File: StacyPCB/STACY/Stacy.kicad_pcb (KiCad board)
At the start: 2 copper layers, 105.4 x 82.6 mm, 48 parts, among them J1 SOL, J10 kill, J11 ext3, J12 push_start, J13 relays, J14 door_lock, J15 ble_hm-10, J16 door_nano, J4 ext4, J5 ext0, J6 ext1, J7 USB_B_Micro, J8 SWD Debug, J9 ext2, SW1 SW_Push, U1 ATSAMD21G18A-AUT, U2 TPS62163DSG, Y1 16MHz

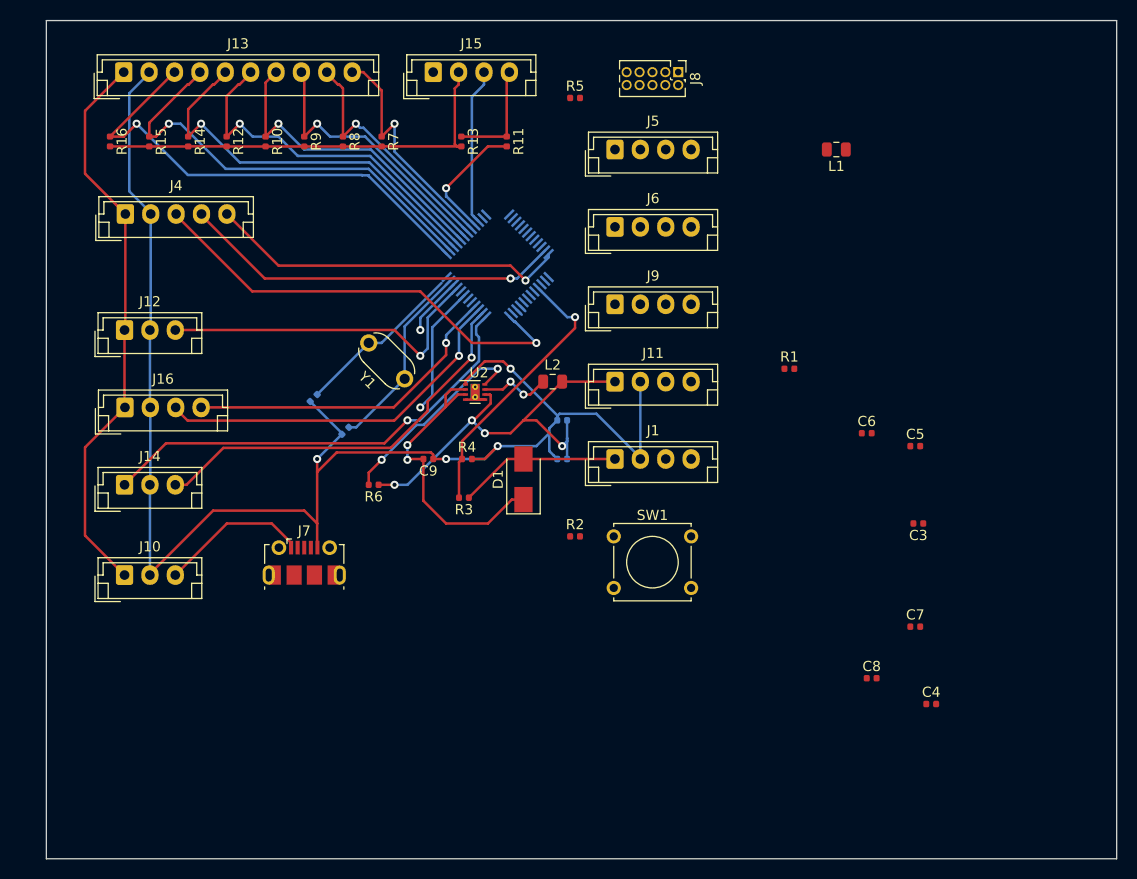
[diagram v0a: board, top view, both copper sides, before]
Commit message: Routed all decoupling caps and fixed clock footprint. This version has been manufactured
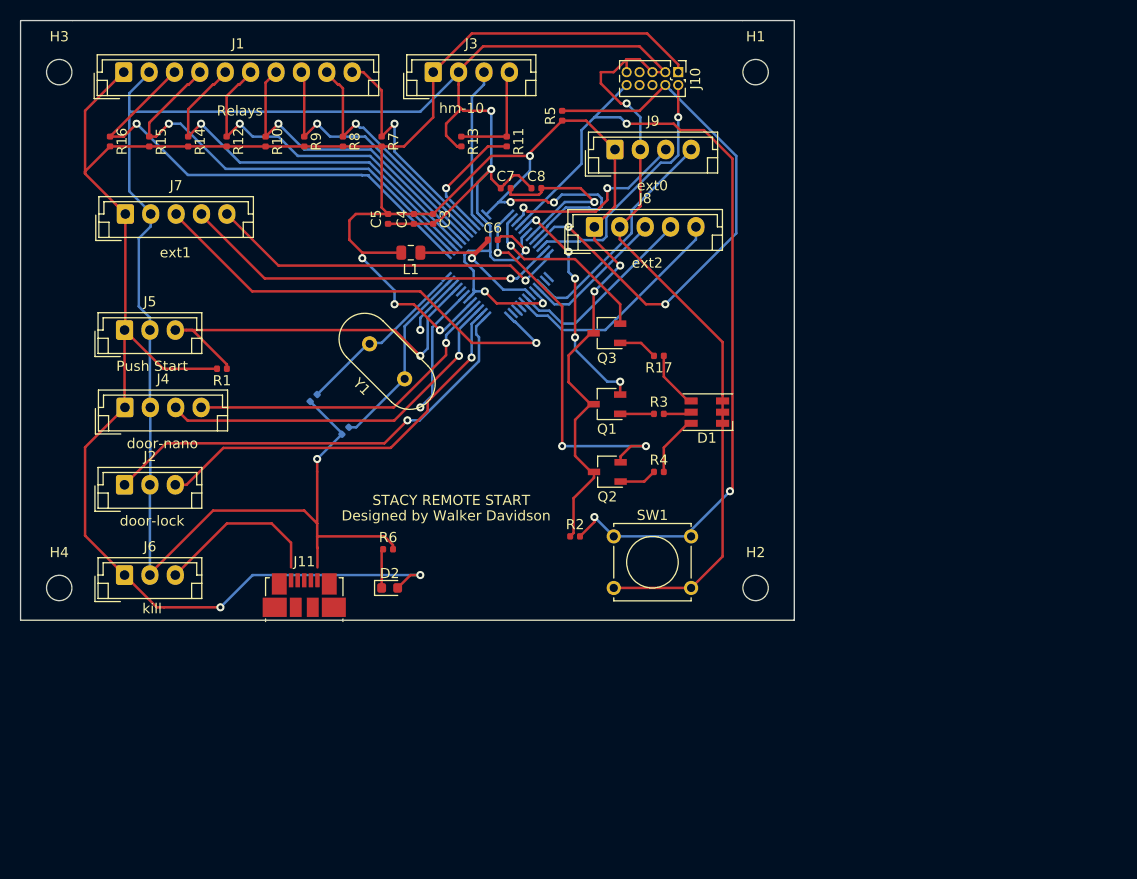
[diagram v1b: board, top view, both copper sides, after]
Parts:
- removed C10, C11, C9: 10u, Capacitor_SMD:C_0402_1005Metric
- removed the J1 at (166.5, 88.9)
- removed the J6 at (166.5, 66.0)
- removed the J7 at (135.9, 99.1)
- removed the J9 at (166.5, 73.7)
- removed L2: 2.2u, Inductor_SMD:L_0805_2012Metric
- removed U2: TPS62163DSG, Package_SON:WSON-8-1EP_2x2mm_P0.5mm_EP0.9x1.6mm_ThermalVias
- added D2: LED, LED_SMD:LED_0603_1608Metric, F.Cu at (144.3, 101.6)
- added H1: MountingHole, MountingHole:MountingHole_2.5mm, F.Cu at (180.3, 50.8)
- added H2: MountingHole, MountingHole:MountingHole_2.5mm, F.Cu at (180.3, 101.6)
- added H3: MountingHole, MountingHole:MountingHole_2.5mm, F.Cu at (111.8, 50.8)
- added H4: MountingHole, MountingHole:MountingHole_2.5mm, F.Cu at (111.8, 101.6)
- added J8: ext2, Connector_JST:JST_EH_B5B-EH-A_1x05_P2.50mm_Vertical, F.Cu at (164.5, 66.0)
- added Q1: 2N2219, Package_TO_SOT_SMD:TSOT-23, F.Cu at (165.7, 83.5)
- added Q2: 2N2219, Package_TO_SOT_SMD:TSOT-23, F.Cu at (165.7, 90.2)
- added Q3: 2N2219, Package_TO_SOT_SMD:TSOT-23, F.Cu at (165.7, 76.5)
- added R17: 220, Resistor_SMD:R_0402_1005Metric, F.Cu at (170.8, 78.7)
- D1: value B160-13-FSMA-M -> LED_RGB; footprint Diode_SMD:D_SMA -> LED_SMD:LED_RGB_PLCC-6
- J11: value ext3 -> USB_B_Micro; footprint Connector_JST:JST_EH_B4B-EH-A_1x04_P2.50mm_Vertical -> Connector_USB:USB_Micro-B_Molex_47346-0001
- J7: renamed from J4; value ext4 -> ext1
- R3: value 10k -> 220
- R4: value 1k -> 220
- R6: value 100k -> 220
- Y1: footprint Crystal:Resonator-2Pin_W6.0mm_H3.0mm -> Crystal:Crystal_HC49-U_Vertical
- moved C4 69.8 mm to (146.7, 65.3), turned to 90 degrees
- moved C7 59.1 mm to (155.7, 62.2)
- moved C8 58.5 mm to (158.8, 62.2)
- moved C5 56.5 mm to (144.1, 65.3), turned to 90 degrees
- moved C3 56.4 mm to (148.6, 65.3), turned to 270 degrees
- moved R1 55.9 mm to (127.8, 80.0), turned to 180 degrees
- moved L1 43.1 mm to (146.4, 68.6)
- moved C6 41.5 mm to (154.5, 67.3)
- moved J11 37.1 mm to (135.9, 102.3)
- moved R3 20.9 mm to (170.8, 84.5), turned to 0 degrees
- moved D1 19.2 mm to (175.5, 84.3), turned to 180 degrees
- moved R4 18.9 mm to (170.8, 90.2)
- moved R6 6.51 mm to (144.1, 97.8), turned to 0 degrees
- moved R5 2.17 mm to (161.3, 55.1), turned to 90 degrees
- renumbered J13 to J1, J8 to J10, J14 to J2, J15 to J3, J16 to J4, J12 to J5, J10 to J6, J5 to J9
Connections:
- D1 pad 1: Net-(C9-Pad2) -> GND
- D1 pad 2: +SOL -> GND
- J11 pad 1: +5V -> kill_sw
- J11 pad 2: GND -> Net-(J11-Pad2)
- J11 pad 3: IO_E3 -> Net-(J11-Pad3)
- J11 pad 4: A03 -> Net-(J11-Pad4)
- R10 pad 2: GND -> +5V
- R12 pad 2: GND -> +5V
- R14 pad 2: GND -> +5V
- R15 pad 2: GND -> +5V
- R16 pad 2: GND -> +5V
- R3 pad 1: +SOL -> Net-(Q1-Pad1)
- R3 pad 2: A01 -> Net-(D1-Pad5)
- R4 pad 1: A01 -> Net-(Q2-Pad1)
- R4 pad 2: GND -> Net-(D1-Pad6)
- R6 pad 1: +5V -> Net-(D2-Pad1)
- R6 pad 2: Net-(R6-Pad2) -> GND
- R7 pad 2: GND -> +5V
- R8 pad 2: GND -> +5V
- R9 pad 2: GND -> +5V
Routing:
- net +5V: track 98.2 -> 306.1 mm, vias 4 -> 10
- net GND: track 194.3 -> 303.4 mm, vias 4 -> 7
- net MCU_RST: track 0.00 -> 85.2 mm, vias 0 -> 3
- net SWD_CLK: track 0.00 -> 55.0 mm, vias 0 -> 2
- net IO_E2: track 0.00 -> 38.3 mm, vias 0 -> 3
- net Net-(C9-Pad2): track 30.1 -> 0.00 mm, vias 2 -> 0
- net SWD_IO: track 0.00 -> 25.3 mm, vias 0 -> 1
- net A03: track 0.00 -> 23.0 mm
- net IO_E1: track 0.00 -> 23.0 mm, vias 0 -> 5
- net A00: track 0.00 -> 22.7 mm
- net Net-(R6-Pad2): track 20.2 -> 0.00 mm, vias 2 -> 0
- net A02: track 0.00 -> 19.2 mm
- net IO_E0: track 0.00 -> 19.2 mm, vias 0 -> 2
- net IO_E3: track 0.00 -> 18.1 mm, vias 0 -> 1
- net Net-(C7-Pad2): track 0.00 -> 17.6 mm, vias 0 -> 1
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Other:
- board size 105.4 x 82.6 mm -> 76.2 x 59.1 mm
- board text added: "Designed by Walker Davidson"
- board text added: "Push Start"
- board text added: "Relays"
- board text added: "STACY REMOTE START"
- board text added: "door-lock"
- board text added: "door-nano"
- board text added: "ext0"
- board text added: "ext1"
- board text added: "ext2"
- board text added: "hm-10"
- board text added: "kill"
